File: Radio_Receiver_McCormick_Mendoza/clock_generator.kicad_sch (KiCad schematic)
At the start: 32 parts, among them J10 CLK_2, J11 I_LO, J12 Q_LO, J24 CLK_0, J9 CLK_1, U5 Si5351A-B-GT, U6 SN74AC74DR, Y1 ASTX-H11-24.576MHZ-T

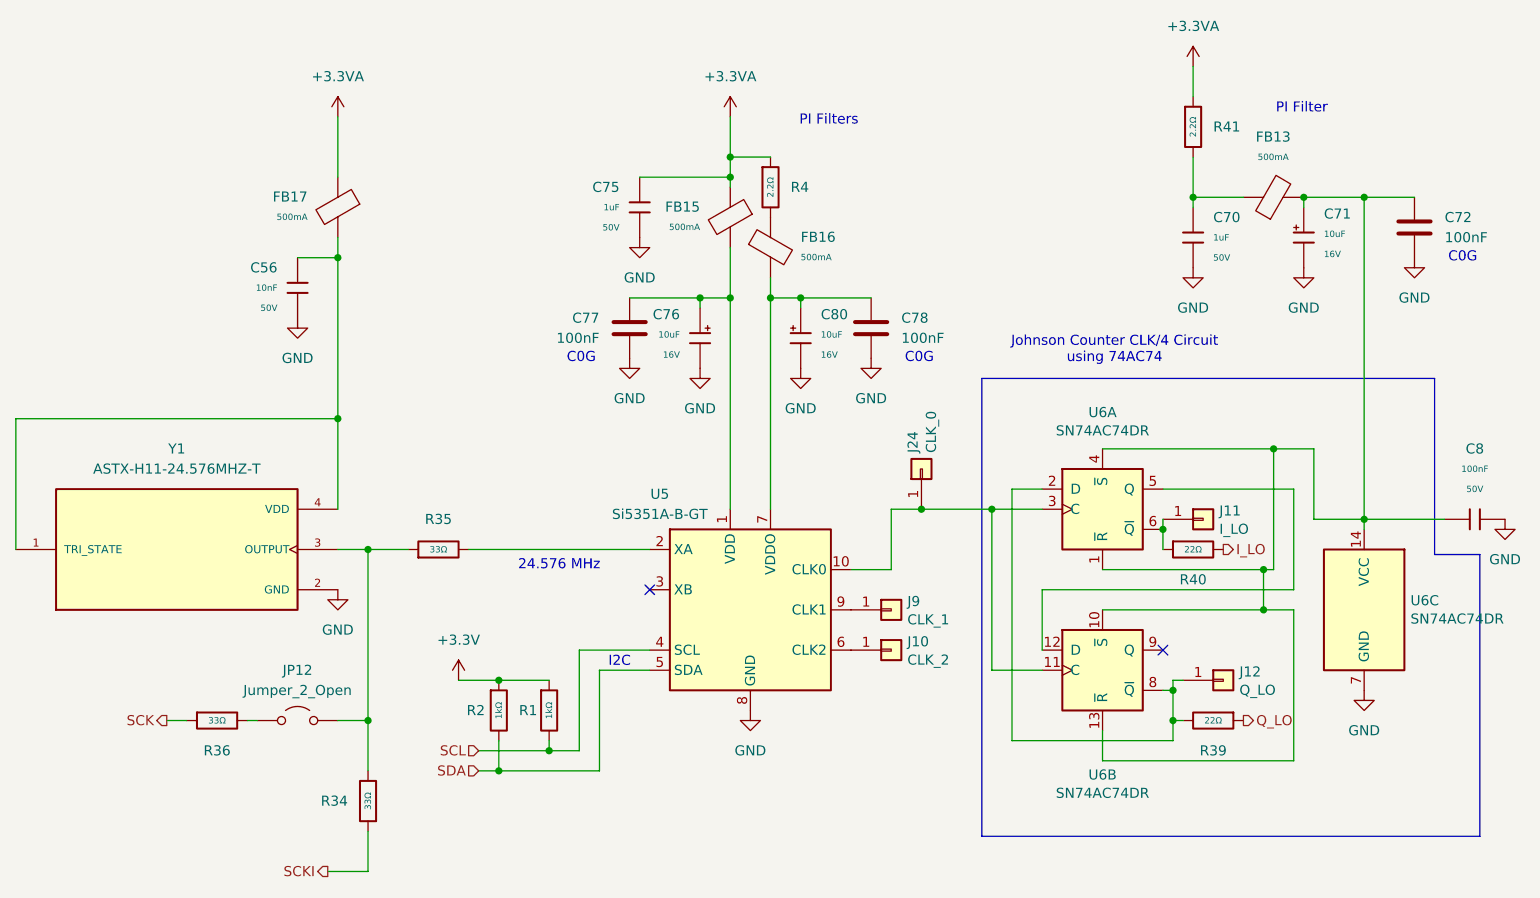
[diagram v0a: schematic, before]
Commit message: Routed antenna and isolated GNDA
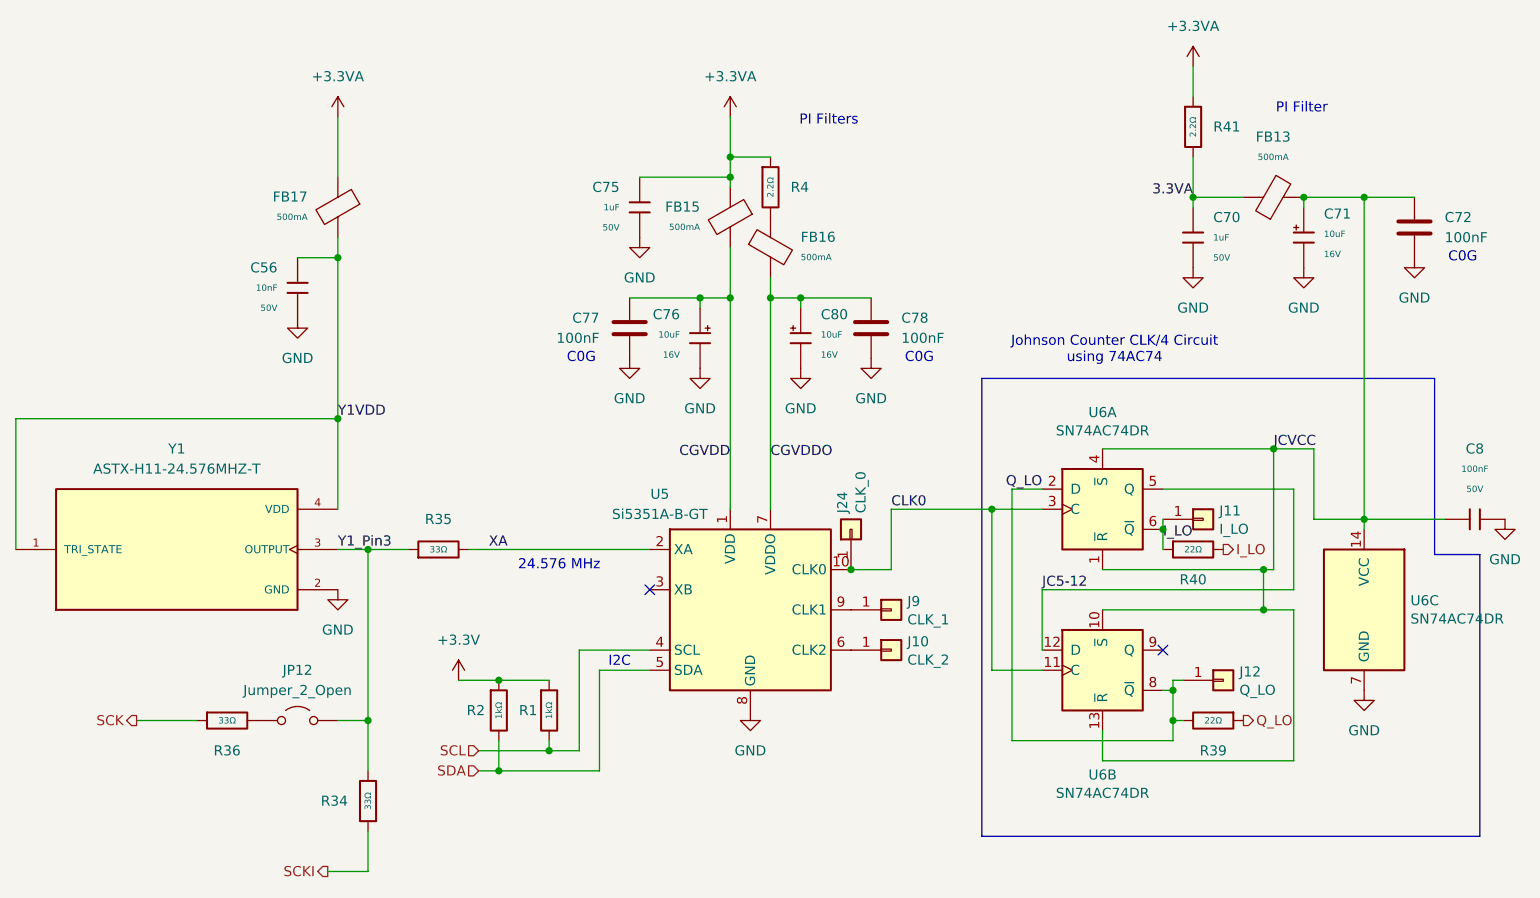
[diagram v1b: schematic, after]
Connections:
- net I_LO: now also J11.1 (Pin_1), R40.1, U6.6 (~{Q})
- net Q_LO: now also J12.1 (Pin_1), R39.2, U6.2 (D), U6.8 (~{Q})
- net CGVDD: now reaches C76.1, C77.1, FB15.2, U5.1 (VDD)
- net 3.3VA: now reaches C70.1, FB13.1, R41.2
- net JCVCC: now reaches C71.1, C72.1, C8.1, FB13.2, U6.1 (~{R}), U6.10 (~{S}), U6.13 (~{R}), U6.14 (VCC), U6.4 (~{S})
- net CLK0: now reaches J24.1 (Pin_1), U5.10 (CLK0), U6.11 (C), U6.3 (C)
- net JC5-12: now reaches U6.12 (D), U6.5 (Q)
- net Y1_Pin3: now reaches JP12.2 (B), R34.2, R35.1, Y1.3 (OUTPUT)
- net CGVDDO: now reaches C78.1, C80.1, FB16.2, U5.7 (VDDO)
- net Y1VDD: now reaches C56.1, FB17.2, Y1.1 (TRI_STATE), Y1.4 (VDD)
- net XA: now reaches R35.2, U5.2 (XA)
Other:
- moved on the sheet: J24, R36
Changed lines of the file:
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@@
 	)
 	(junction
-		(at 137.16 81.28)
-		(diameter 0)
-		(color 0 0 0 0)
-	)
-	(junction
 		(at 113.03 39.37)
 		(diameter 0)
@@
 	)
 	(junction
+		(at 128.27 88.9)
+		(diameter 0)
+		(color 0 0 0 0)
+	)
+	(junction
 		(at 168.91 107.95)
 		(diameter 0)
@@
 	(wire
 		(pts
-			(xy 52.07 107.95) (xy 53.34 107.95)
-		)
-		(stroke
-			(width 0)
-			(type default)
-		)
-	)
-	(wire
-		(pts
-			(xy 137.16 81.28) (xy 146.05 81.28)
-		)
-		(stroke
-			(width 0)
-			(type default)
-		)
-	)
-	(wire
-		(pts
 			(xy 160.02 113.03) (xy 184.15 113.03)
 		)
@@
 	(wire
 		(pts
-			(xy 133.35 88.9) (xy 133.35 81.28)
-		)
-		(stroke
-			(width 0)
-			(type default)
-		)
-	)
-	(wire
-		(pts
 			(xy 171.45 36.83) (xy 171.45 41.91)
 		)
@@
 	(wire
 		(pts
-			(xy 44.45 107.95) (xy 41.91 107.95)
+			(xy 63.5 86.36) (xy 67.31 86.36)
 		)
 		(stroke
@@
 	(wire
 		(pts
-			(xy 63.5 86.36) (xy 67.31 86.36)
+			(xy 63.5 31.75) (xy 63.5 39.37)
 		)
 		(stroke
@@
 		)
 	)
-	(wire
+	(polyline
 		(pts
-			(xy 63.5 31.75) (xy 63.5 39.37)
+			(xy 201.93 86.995) (xy 201.93 64.77)
 		)
 		(stroke
@@
 		)
 	)
-	(polyline
+	(wire
 		(pts
-			(xy 201.93 86.995) (xy 201.93 64.77)
+			(xy 133.35 88.9) (xy 133.35 81.28)
 		)
 		(stroke
@@
 	(wire
 		(pts
-			(xy 133.35 81.28) (xy 137.16 81.28)
+			(xy 38.1 107.95) (xy 45.72 107.95)
 		)
 		(stroke
@@
 		)
 	)
+	(wire
+		(pts
+			(xy 133.35 81.28) (xy 146.05 81.28)
+		)
+		(stroke
+			(width 0)
+			(type default)
+		)
+	)
 	(polyline
 		(pts
@@
 		)
 	)
+	(label "3.3VA"
+		(at 171.45 41.91 180)
+		(effects
+			(font
+				(size 1.27 1.27)
+			)
+			(justify right bottom)
+		)
+	)
+	(label "Q_LO"
+		(at 152.4 78.74 180)
+		(effects
+			(font
+				(size 1.27 1.27)
+			)
+			(justify right bottom)
+		)
+	)
+	(label "CGVDDO"
+		(at 118.11 74.93 0)
+		(effects
+			(font
+				(size 1.27 1.27)
+			)
+			(justify left bottom)
+		)
+	)
+	(label "JC5-12"
+		(at 152.4 91.44 0)
+		(effects
+			(font
+				(size 1.27 1.27)
+			)
+			(justify left bottom)
+		)
+	)
+	(label "JCVCC"
+		(at 181.61 73.66 0)
+		(effects
+			(font
+				(size 1.27 1.27)
+			)
+			(justify left bottom)
+		)
+	)
+	(label "CGVDD"
+		(at 113.03 74.93 180)
+		(effects
+			(font
+				(size 1.27 1.27)
+			)
+			(justify right bottom)
+		)
+	)
+	(label "I_LO"
+		(at 167.64 85.09 0)
+		(effects
+			(font
+				(size 1.27 1.27)
+			)
+			(justify left bottom)
+		)
+	)
+	(label "CLK0"
+		(at 133.35 81.28 0)
+		(effects
+			(font
+				(size 1.27 1.27)
+			)
+			(justify left bottom)
+		)
+	)
+	(label "Y1VDD"
+		(at 63.5 69.85 0)
+		(effects
+			(font
+				(size 1.27 1.27)
+			)
+			(justify left bottom)
+		)
+	)
+	(label "XA"
+		(at 82.55 86.36 0)
+		(effects
+			(font
+				(size 1.27 1.27)
+			)
+			(justify left bottom)
+		)
+	)
+	(label "Y1_Pin3"
+		(at 63.5 86.36 0)
+		(effects
+			(font
+				(size 1.27 1.27)
+			)
+			(justify left bottom)
+		)
+	)
 	(hierarchical_label "I_LO"
 		(shape output)
@@
 	(hierarchical_label "SCK"
 		(shape output)
-		(at 41.91 107.95 180)
+		(at 38.1 107.95 180)
 		(effects
 			(font
@@
 	(symbol
 		(lib_id "PCM_JLCPCB-Resistors:0805,33Ω")
-		(at 48.26 107.95 90)
+		(at 49.53 107.95 90)
 		(mirror x)
 		(unit 1)
@@
 		(dnp no)
 		(property "Reference" "R36"
-			(at 48.26 111.76 90)
+			(at 49.53 111.76 90)
 			(show_name no)
 			(do_not_autoplace no)
@@
 		)
 		(property "Value" "33Ω"
-			(at 48.26 107.95 90)
+			(at 49.53 107.95 90)
 			(show_name no)
 			(do_not_autoplace yes)
@@
 		)
 		(property "Footprint" "PCM_JLCPCB:R_0805"
-			(at 48.26 106.172 90)
+			(at 49.53 106.172 90)
 			(hide yes)
 			(show_name no)
@@
 		)
 		(property "Datasheet" "https://www.lcsc.com/datasheet/lcsc_datasheet_2205311830_UNI-ROYAL-Uniroyal-Elec-0805W8F330JT5E_C17634.pdf"
-			(at 48.26 107.95 0)
+			(at 49.53 107.95 0)
 			(hide yes)
 			(show_name no)
@@
 		)
 		(property "Description" "125mW Thick Film Resistors 150V ±1% ±200ppm/°C 33Ω 0805 Chip Resistor - Surface Mount ROHS"
-			(at 48.26 107.95 0)
+			(at 49.53 107.95 0)
 			(hide yes)
 			(show_name no)
@@
 		)
 		(property "LCSC" "C17634"
-			(at 48.26 107.95 0)
+			(at 49.53 107.95 0)
 			(hide yes)
 			(show_name no)
@@
 		)
 		(property "Stock" "335994"
-			(at 48.26 107.95 0)
+			(at 49.53 107.95 0)
 			(hide yes)
 			(show_name no)
@@
 		)
 		(property "Price" "0.005USD"
-			(at 48.26 107.95 0)
+			(at 49.53 107.95 0)
 			(hide yes)
 			(show_name no)
@@
 		)
 		(property "Process" "SMT"
-			(at 48.26 107.95 0)
+			(at 49.53 107.95 0)
 			(hide yes)
 			(show_name no)
@@
 		)
 		(property "Minimum Qty" "20"
-			(at 48.26 107.95 0)
+			(at 49.53 107.95 0)
 			(hide yes)
 			(show_name no)
@@
 		)
 		(property "Attrition Qty" "10"
-			(at 48.26 107.95 0)
+			(at 49.53 107.95 0)
 			(hide yes)
 			(show_name no)
@@
 		)
 		(property "Class" "Basic Component"
-			(at 48.26 107.95 0)
+			(at 49.53 107.95 0)
 			(hide yes)
 			(show_name no)
@@
 		)
 		(property "Category" "Resistors,Chip Resistor - Surface Mount"
-			(at 48.26 107.95 0)
+			(at 49.53 107.95 0)
 			(hide yes)
 			(show_name no)
@@
 		)
 		(property "Part" "0805W8F330JT5E"
-			(at 48.26 107.95 0)
+			(at 49.53 107.95 0)
 			(hide yes)
 			(show_name no)
@@
 		)
 		(property "Resistance" "33Ω"
-			(at 48.26 107.95 0)
+			(at 49.53 107.95 0)
 			(hide yes)
 			(show_name no)
@@
 		)
 		(property "Power(Watts)" "125mW"
-			(at 48.26 107.95 0)
+			(at 49.53 107.95 0)
 			(hide yes)
 			(show_name no)
@@
 		)
 		(property "Type" "Thick Film Resistors"
-			(at 48.26 107.95 0)
+			(at 49.53 107.95 0)
 			(hide yes)
 			(show_name no)
@@
 		)
 		(property "Overload Voltage (Max)" "150V"
-			(at 48.26 107.95 0)
+			(at 49.53 107.95 0)
 			(hide yes)
 			(show_name no)
@@
 		)
 		(property "Operating Temperature Range" "-55°C~+155°C"
-			(at 48.26 107.95 0)
+			(at 49.53 107.95 0)
 			(hide yes)
 			(show_name no)
@@
 		)
 		(property "Tolerance" "±1%"
-			(at 48.26 107.95 0)
+			(at 49.53 107.95 0)
 			(hide yes)
 			(show_name no)
@@
 		)
 		(property "Temperature Coefficient" "±200ppm/°C"
-			(at 48.26 107.95 0)
+			(at 49.53 107.95 0)
 			(hide yes)
 			(show_name no)
@@
 	(symbol
 		(lib_id "Connector_Generic:Conn_01x01")
-		(at 137.16 76.2 90)
+		(at 128.27 83.82 90)
 		(unit 1)
 		(body_style 1)
@@
 		(dnp no)
 		(property "Reference" "J24"
-			(at 136.0932 74.168 0)
+			(at 127.2032 81.788 0)
 			(show_name no)
 			(do_not_autoplace no)
@@
 		)
 		(property "Value" "CLK_0"
-			(at 138.4046 74.168 0)
+			(at 129.5146 81.788 0)
 			(show_name no)
 			(do_not_autoplace no)
@@
 		)
 		(property "Footprint" "Connector_PinHeader_2.54mm:PinHeader_1x01_P2.54mm_Vertical"
-			(at 137.16 76.2 0)
+			(at 128.27 83.82 0)
 			(hide yes)
 			(show_name no)
@@
 		)
 		(property "Datasheet" "~"
-			(at 137.16 76.2 0)
+			(at 128.27 83.82 0)
 			(hide yes)
 			(show_name no)
@@
 		)
 		(property "Description" ""
-			(at 137.16 76.2 0)
+			(at 128.27 83.82 0)
 			(show_name no)
 			(do_not_autoplace no)

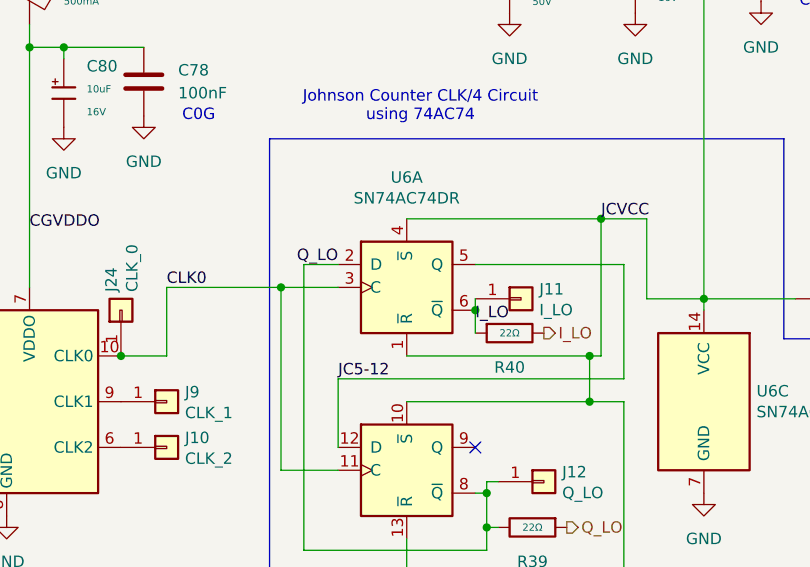
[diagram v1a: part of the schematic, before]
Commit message: Finished routing master copy and added GND and PWR planes with vias
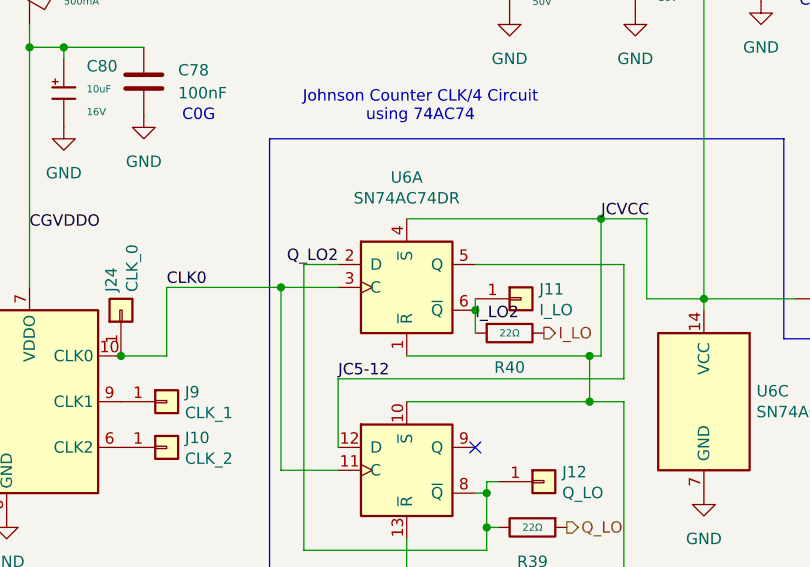
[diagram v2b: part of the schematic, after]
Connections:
- net I_LO: no longer J11.1 (Pin_1), R40.1, U6.6 (~{Q})
- net Q_LO: no longer J12.1 (Pin_1), R39.2, U6.2 (D), U6.8 (~{Q})
- new net I_LO2: J11.1 (Pin_1), R40.1, U6.6 (~{Q})
- new net Q_LO2: J12.1 (Pin_1), R39.2, U6.2 (D), U6.8 (~{Q})
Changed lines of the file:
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@@
 		)
 	)
-	(label "Q_LO"
+	(label "Q_LO2"
 		(at 152.4 78.74 180)
 		(effects
@@
 		)
 	)
-	(label "I_LO"
+	(label "I_LO2"
 		(at 167.64 85.09 0)
 		(effects
